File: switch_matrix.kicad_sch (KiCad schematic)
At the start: 0 parts

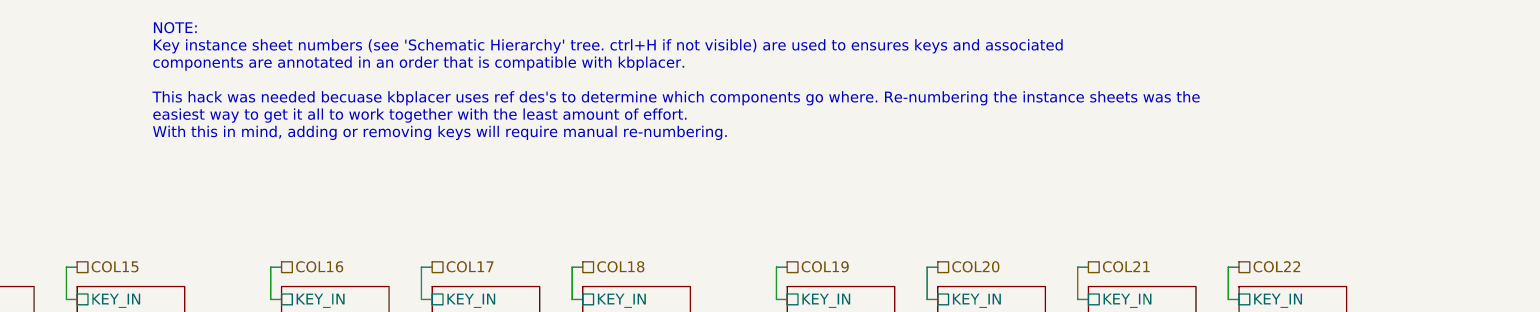
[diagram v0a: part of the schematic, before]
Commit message: created dev-board to prove design before full-size
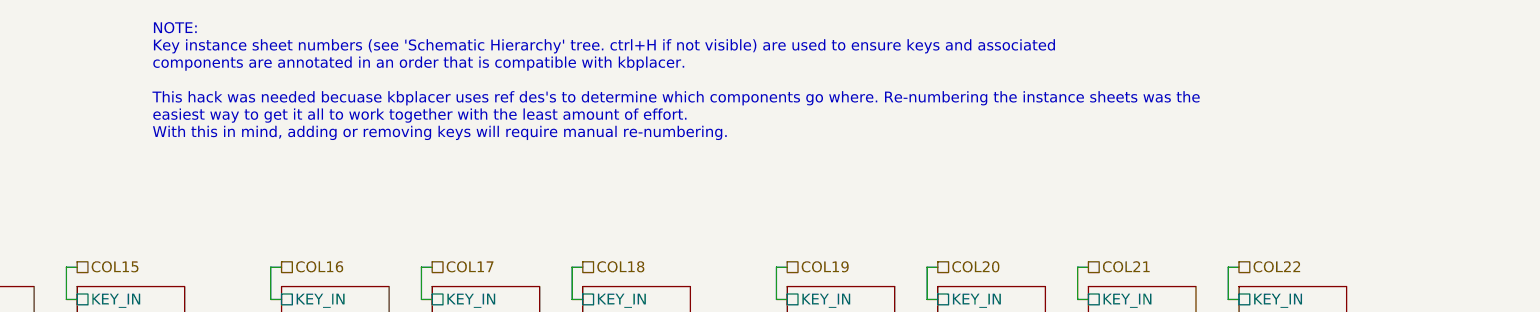
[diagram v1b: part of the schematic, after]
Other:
- note added: "NOTE: Key instance sheet numbers (see 'Schematic Hierarchy' tree. ctrl+H if not visible) are used to ensure keys and associated components are annotated in an order that is compatible with kbplacer. This hack was needed becuase kbplacer uses ref des's to determine which components go where. Re-numbering the instance sheets was the easiest way to get it all to work together with the least amount o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"
- note removed: "NOTE: Key instance sheet numbers (see 'Schematic Hierarchy' tree. ctrl+H if not visible) are used to ensures keys and associated components are annotated in an order that is compatible with kbplacer. This hack was needed becuase kbplacer uses ref des's to determine which components go where. Re-numbering the instance sheets was the easiest way to get it all to work together with the least amount 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"
